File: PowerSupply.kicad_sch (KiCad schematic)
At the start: 13 parts, among them J1 Jack-DC, U3 MAX1044CPA+

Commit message: using smt caps and resistors
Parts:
- R24, R25: footprint Resistor_THT:R_Axial_DIN0207_L6.3mm_D2.5mm_P10.16mm_Horizontal -> Resistor_SMD:R_0805_2012Metric_Pad1.20x1.40mm_HandSolder
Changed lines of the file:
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@@
 			)
 		)
-		(property "Footprint" "Resistor_THT:R_Axial_DIN0207_L6.3mm_D2.5mm_P10.16mm_Horizontal"
+		(property "Footprint" "Resistor_SMD:R_0805_2012Metric_Pad1.20x1.40mm_HandSolder"
 			(at 216.027 81.28 90)
 			(effects
@@
 			)
 		)
-		(property "Footprint" "Resistor_THT:R_Axial_DIN0207_L6.3mm_D2.5mm_P10.16mm_Horizontal"
+		(property "Footprint" "Resistor_SMD:R_0805_2012Metric_Pad1.20x1.40mm_HandSolder"
 			(at 216.027 96.52 90)
 			(effects

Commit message: change metal film resistor footprint
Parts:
- C16, C21: footprint Capacitor_THT:CP_Radial_D5.0mm_P2.00mm -> Capacitor_SMD:CP_Elec_5x5.4
- C17, C18, C19, C20: footprint Capacitor_THT:CP_Radial_D5.0mm_P2.00mm -> Capacitor_SMD:CP_Elec_4x5.4
- U3: footprint ECE319K:DIP-8_W7.62mm_LongPads -> Package_SO:SO-8_3.9x4.9mm_P1.27mm
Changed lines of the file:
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@@
 			)
 		)
-		(property "Footprint" "Capacitor_THT:CP_Radial_D5.0mm_P2.00mm"
+		(property "Footprint" "Capacitor_SMD:CP_Elec_4x5.4"
 			(at 200.3298 98.425 0)
 			(effects
@@
 			)
 		)
-		(property "Footprint" "Capacitor_THT:CP_Radial_D5.0mm_P2.00mm"
+		(property "Footprint" "Capacitor_SMD:CP_Elec_5x5.4"
 			(at 98.7552 86.36 0)
 			(effects
@@
 			)
 		)
-		(property "Footprint" "ECE319K:DIP-8_W7.62mm_LongPads"
+		(property "Footprint" "Package_SO:SO-8_3.9x4.9mm_P1.27mm"
 			(at 158.115 86.36 0)
 			(effects
@@
 			)
 		)
-		(property "Footprint" "Capacitor_THT:CP_Radial_D5.0mm_P2.00mm"
+		(property "Footprint" "Capacitor_SMD:CP_Elec_5x5.4"
 			(at 230.2002 100.33 0)
 			(effects
@@
 			)
 		)
-		(property "Footprint" "Capacitor_THT:CP_Radial_D5.0mm_P2.00mm"
+		(property "Footprint" "Capacitor_SMD:CP_Elec_4x5.4"
 			(at 142.24 94.2848 0)
 			(effects
@@
 			)
 		)
-		(property "Footprint" "Capacitor_THT:CP_Radial_D5.0mm_P2.00mm"
+		(property "Footprint" "Capacitor_SMD:CP_Elec_4x5.4"
 			(at 152.4 101.9048 0)
 			(effects
@@
 			)
 		)
-		(property "Footprint" "Capacitor_THT:CP_Radial_D5.0mm_P2.00mm"
+		(property "Footprint" "Capacitor_SMD:CP_Elec_4x5.4"
 			(at 121.6152 97.79 0)
 			(effects

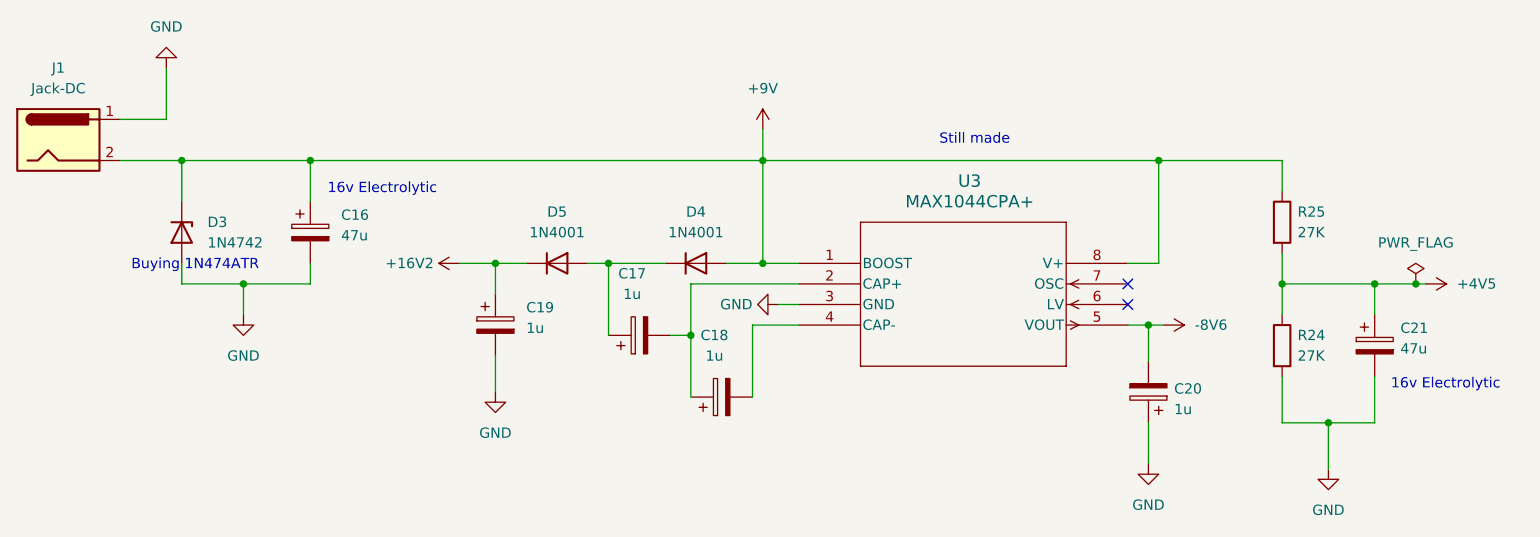
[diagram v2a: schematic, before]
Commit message: add all smd components
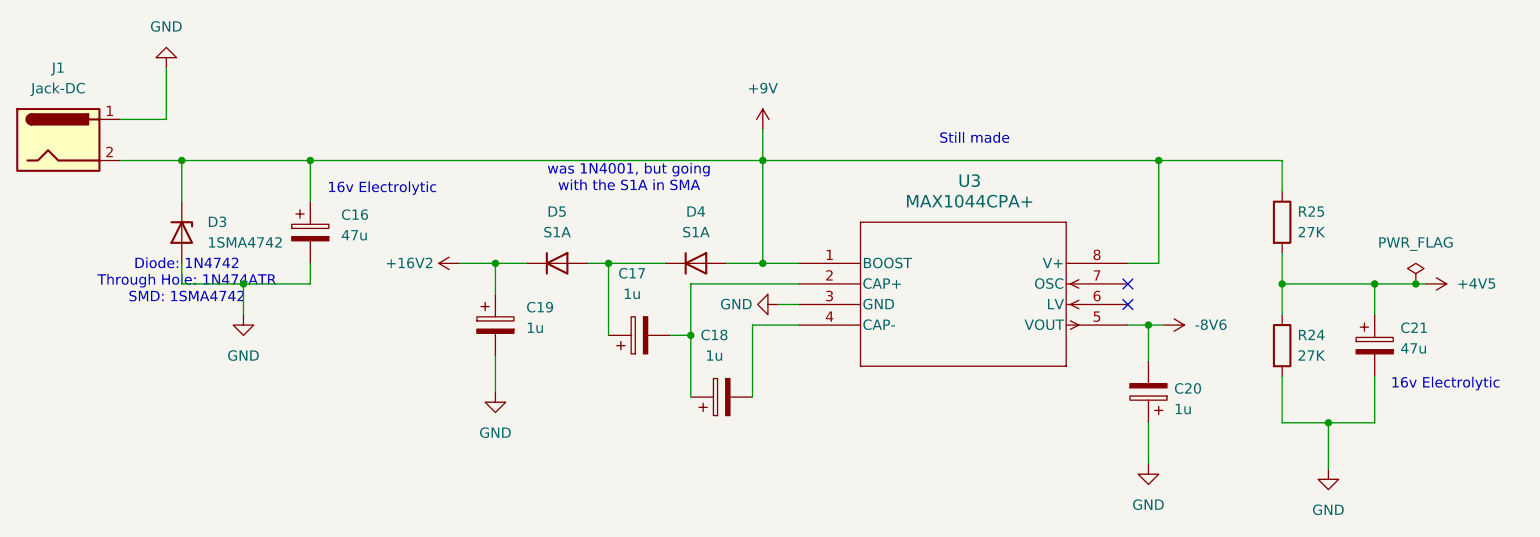
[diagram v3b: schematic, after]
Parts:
- D3: value 1N4742 -> 1SMA4742; footprint Diode_THT:D_DO-41_SOD81_P10.16mm_Horizontal -> Diode_SMD:D_SMA_Handsoldering
- D4, D5: value 1N4001 -> S1A; footprint Diode_THT:D_DO-41_SOD81_P10.16mm_Horizontal -> Diode_SMD:D_SMA_Handsoldering
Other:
- note added: "Diode: 1N4742 Through Hole: 1N474ATR SMD: 1SMA4742"
- note added: "was 1N4001, but going with the S1A in SMA"
- note removed: "Buying 1N474ATR"
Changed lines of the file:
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@@
+		)
+	)
+	(text "was 1N4001, but going\nwith the S1A in SMA"
+		(exclude_from_sim no)
+		(at 137.16 75.946 0)
+		(effects
+			(font
+				(size 1.27 1.27)
+			)
 		)
 	)
@@
 		)
 	)
-	(text "Buying 1N474ATR\n"
-		(exclude_from_sim no)
-		(at 83.566 86.614 0)
+	(text "Diode: 1N4742\nThrough Hole: 1N474ATR\nSMD: 1SMA4742\n"
+		(exclude_from_sim no)
+		(at 82.55 88.646 0)
 		(effects
 			(font
@@
 			)
 		)
-		(property "Value" "1N4001"
+		(property "Value" "S1A"
 			(at 145.415 82.55 0)
 			(effects
@@
 			)
 		)
-		(property "Footprint" "Diode_THT:D_DO-41_SOD81_P10.16mm_Horizontal"
+		(property "Footprint" "Diode_SMD:D_SMA_Handsoldering"
 			(at 145.415 86.36 0)
 			(effects
@@
 			)
 		)
-		(property "Value" "1N4742"
+		(property "Value" "1SMA4742"
 			(at 85.09 83.8199 90)
 			(effects
@@
 			)
 		)
-		(property "Footprint" "Diode_THT:D_DO-41_SOD81_P10.16mm_Horizontal"
+		(property "Footprint" "Diode_SMD:D_SMA_Handsoldering"
 			(at 77.47 82.55 0)
 			(effects
@@
 			)
 		)
-		(property "Value" "1N4001"
+		(property "Value" "S1A"
 			(at 128.27 82.55 0)
 			(effects
@@
 			)
 		)
-		(property "Footprint" "Diode_THT:D_DO-41_SOD81_P10.16mm_Horizontal"
+		(property "Footprint" "Diode_SMD:D_SMA_Handsoldering"
 			(at 128.27 86.36 0)
 			(effects
